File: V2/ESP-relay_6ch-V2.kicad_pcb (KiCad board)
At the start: 2 copper layers, 173 x 67.8 mm, 104 parts, among them J1 24VDC, J2 24V INPUTS, J3 OUT1, J4 OUT1, J5 OUT1, J6 OUT1, J7 OUT1, J8 OUT1, K1 G5PZ-1A, K2 G5PZ-1A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

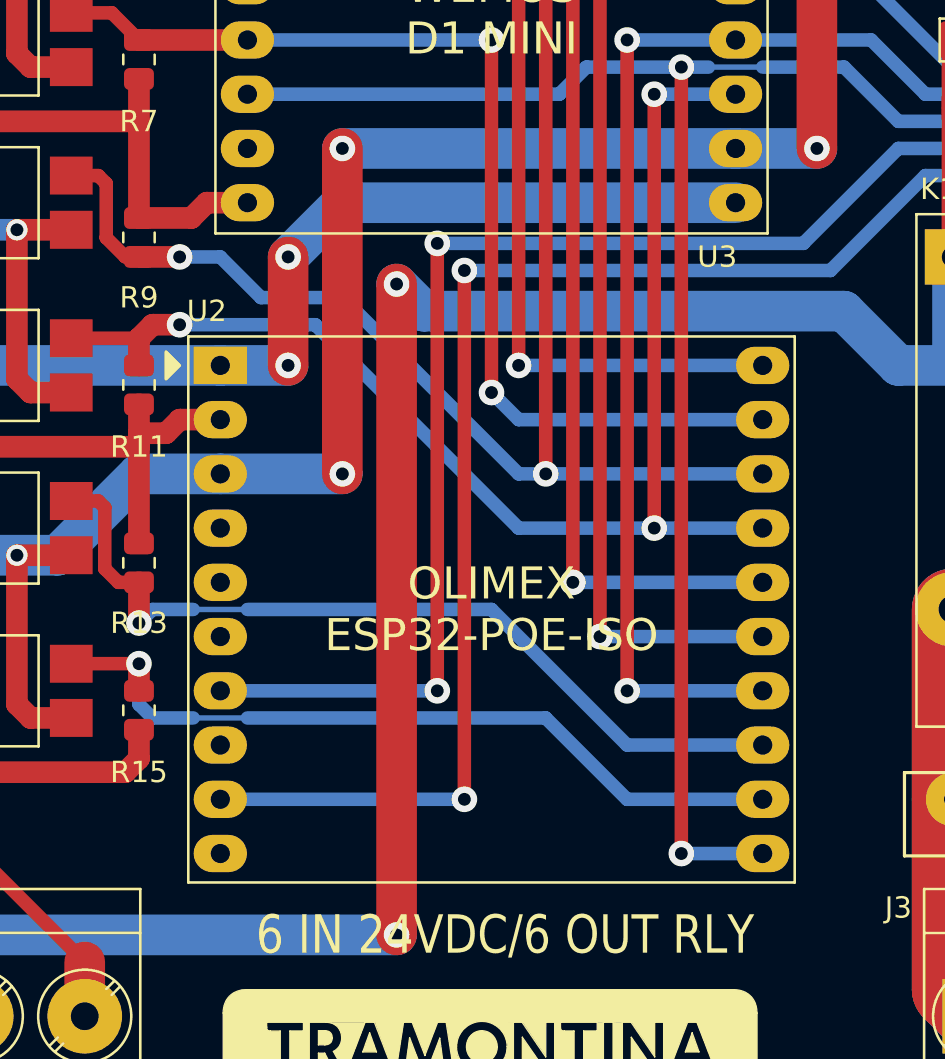
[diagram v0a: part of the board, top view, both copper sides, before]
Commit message: footprint updates
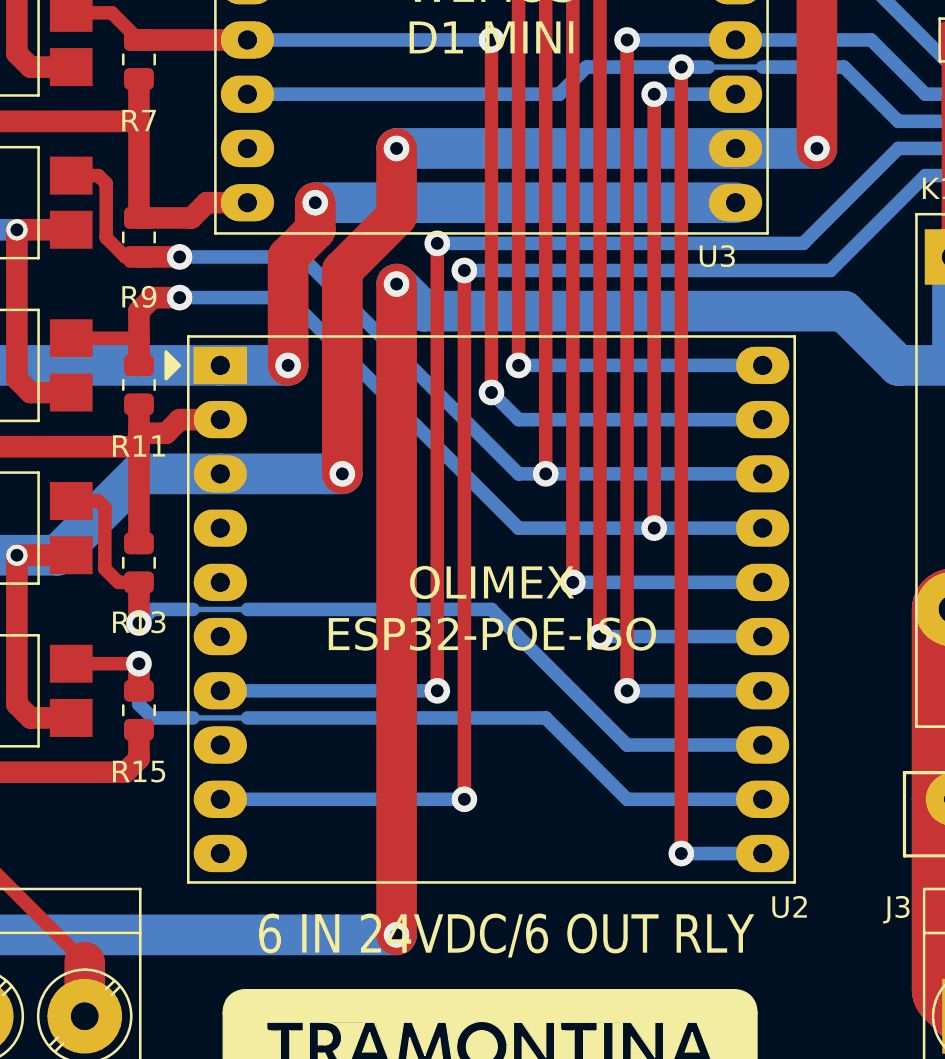
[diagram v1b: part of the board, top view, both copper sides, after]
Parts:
- U4, U5, U6, U7, U8, U9: footprint Tales:SMDIP-4_W9.53mm -> Package_DIP:SMDIP-4_W9.53mm
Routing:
- net /32-GPI34: track 62.0 -> 63.8 mm
- net GNDREF: track 440.8 -> 439.4 mm
- net +5V: track 121.0 -> 121.7 mm

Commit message: work in progress
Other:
- board text added: "6x IN 24VDC/6x OUT RLY"
- board text added: "MAX LOAD 10 A PER CHANNEL"
- board text removed: "6 IN 24VDC/6 OUT RLY"
- board text removed: "MAXIMUM 10 A PER CHANNEL"
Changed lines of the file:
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@@
     (tags "Diode Mini-MELF (SOD-80)")
     (property "Case" "MiniMELF")
-    (property "JLCPCB BOM" "0")
-    (property "Mfr" "Rectron")
+    (property "JLCPCB BOM" "1")
+    (property "LCSC Part" "C109072")
+    (property "Mfr" "Semtech")
     (property "Mfr PN" "ZMM5239B")
     (property "Sheetfile" "ESP-relay_6ch-V2.kicad_sch")
     (property "Sheetname" "")
     (property "Technology" "~")
-    (property "Vendor" "Mouser")
-    (property "Vendor PN" "583-ZMM5239B")
+    (property "Vendor" "JLCPCB")
+    (property "Vendor PN" "C109072")
     (attr smd)
     (fp_text reference "D10" (at 3.655 0 180) (layer "F.SilkS")
@@
     (tags "Diode Mini-MELF (SOD-80)")
     (property "Case" "MiniMELF")
-    (property "JLCPCB BOM" "0")
-    (property "Mfr" "Rectron")
+    (property "JLCPCB BOM" "1")
+    (property "LCSC Part" "C109072")
+    (property "Mfr" "Semtech")
     (property "Mfr PN" "ZMM5239B")
     (property "Sheetfile" "ESP-relay_6ch-V2.kicad_sch")
     (property "Sheetname" "")
     (property "Technology" "~")
-    (property "Vendor" "Mouser")
-    (property "Vendor PN" "583-ZMM5239B")
+    (property "Vendor" "JLCPCB")
+    (property "Vendor PN" "C109072")
     (attr smd)
     (fp_text reference "D7" (at 3.655 0 180) (layer "F.SilkS")
@@
     (tags "Diode Mini-MELF (SOD-80)")
     (property "Case" "MiniMELF")
-    (property "JLCPCB BOM" "0")
-    (property "Mfr" "Rectron")
+    (property "JLCPCB BOM" "1")
+    (property "LCSC Part" "C109072")
+    (property "Mfr" "Semtech")
     (property "Mfr PN" "ZMM5239B")
     (property "Sheetfile" "ESP-relay_6ch-V2.kicad_sch")
     (property "Sheetname" "")
     (property "Technology" "~")
-    (property "Vendor" "Mouser")
-    (property "Vendor PN" "583-ZMM5239B")
+    (property "Vendor" "JLCPCB")
+    (property "Vendor PN" "C109072")
     (attr smd)
     (fp_text reference "D9" (at 3.655 0 180) (layer "F.SilkS")
@@
     (tags "Diode Mini-MELF (SOD-80)")
     (property "Case" "MiniMELF")
-    (property "JLCPCB BOM" "0")
-    (property "Mfr" "Rectron")
+    (property "JLCPCB BOM" "1")
+    (property "LCSC Part" "C109072")
+    (property "Mfr" "Semtech")
     (property "Mfr PN" "ZMM5239B")
     (property "Sheetfile" "ESP-relay_6ch-V2.kicad_sch")
     (property "Sheetname" "")
     (property "Technology" "~")
-    (property "Vendor" "Mouser")
-    (property "Vendor PN" "583-ZMM5239B")
+    (property "Vendor" "JLCPCB")
+    (property "Vendor PN" "C109072")
     (attr smd)
     (fp_text reference "D8" (at 3.655 0 180) (layer "F.SilkS")
@@
     (tags "Diode Mini-MELF (SOD-80)")
     (property "Case" "MiniMELF")
-    (property "JLCPCB BOM" "0")
-    (property "Mfr" "Rectron")
+    (property "JLCPCB BOM" "1")
+    (property "LCSC Part" "C109072")
+    (property "Mfr" "Semtech")
     (property "Mfr PN" "ZMM5239B")
     (property "Sheetfile" "ESP-relay_6ch-V2.kicad_sch")
     (property "Sheetname" "")
     (property "Technology" "~")
-    (property "Vendor" "Mouser")
-    (property "Vendor PN" "583-ZMM5239B")
+    (property "Vendor" "JLCPCB")
+    (property "Vendor PN" "C109072")
     (attr smd)
     (fp_text reference "D5" (at 3.655 0 180) (layer "F.SilkS")
@@
     (tags "Diode Mini-MELF (SOD-80)")
     (property "Case" "MiniMELF")
-    (property "JLCPCB BOM" "0")
-    (property "Mfr" "Rectron")
+    (property "JLCPCB BOM" "1")
+    (property "LCSC Part" "C109072")
+    (property "Mfr" "Semtech")
     (property "Mfr PN" "ZMM5239B")
     (property "Sheetfile" "ESP-relay_6ch-V2.kicad_sch")
     (property "Sheetname" "")
     (property "Technology" "~")
-    (property "Vendor" "Mouser")
-    (property "Vendor PN" "583-ZMM5239B")
+    (property "Vendor" "JLCPCB")
+    (property "Vendor PN" "C109072")
     (attr smd)
     (fp_text reference "D6" (at 3.655 0 180) (layer "F.SilkS")
@@
   (gr_line (start 73.66 76.2) (end 88.9 76.2) (layer "F.SilkS") (width 0.15))
   (gr_rect (start 64.77 64.28) (end 237.77 132.08) (layer "Edge.Cuts") (width 0.1) (fill none))
-  (gr_text "MAXIMUM 10 A PER CHANNEL" (at 193.675 97.79) (layer "B.Cu")
-    (effects (font (size 2.8 2.5) (thickness 0.4)) (justify mirror))
-  )
   (gr_text "-" (at 78.74 130.302) (layer "F.SilkS")
     (effects (font (size 2 2) (thickness 0.5)))
@@
     (effects (font (size 1.8 1.6) (thickness 0.3)) (justify left))
   )
-  (gr_text "6 IN 24VDC/6 OUT RLY" (at 133.985 119.38) (layer "F.SilkS")
+  (gr_text "MAX LOAD 10 A PER CHANNEL" (at 193.04 67.945) (layer "F.SilkS")
+    (effects (font (size 2.3 2) (thickness 0.3)))
+  )
+  (gr_text "6x IN 24VDC/6x OUT RLY" (at 133.985 119.38) (layer "F.SilkS")
     (effects (font (size 1.8 1.5) (thickness 0.3)))
   )

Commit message: wip
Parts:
- removed the J1 at (72.4, 123.2)
- removed REF**: Logo_Tramontina_25mm, Tales:Logo_Tramontina_25mm
- J1: renamed from J2; value 24V INPUTS -> POWER & INPUTS; footprint Tales:TerminalBlock_Phoenix_MKDS-3-6-5.08_1x06_P5.08mm_Horizontal -> Tales:TerminalBlock_Phoenix_MKDS-3-8-5.08_1x08_P5.08mm_Horizontal
- moved C2 19.3 mm to (74.5, 82.5)
- moved J1 11.4 mm to (78.7, 118.1)
- moved D1 5.24 mm to (83.8, 108.8)
- moved R28 5.24 mm to (80.4, 109.2)
- moved R29 5.24 mm to (80.4, 106.7)
- moved R30 5.24 mm to (76.6, 109.2)
- moved R31 5.24 mm to (76.6, 106.7)
- moved R32 5.24 mm to (72.7, 109.2)
- moved R33 5.24 mm to (72.7, 106.7)
- moved R34 5.24 mm to (68.9, 109.2)
- moved R35 5.24 mm to (68.9, 106.7)
- moved D23 5.08 mm to (72.0, 101.6)
- moved D24 5.08 mm to (79.6, 101.6)
- moved J2 5.08 mm to (156.2, 118.1)
- moved J3 5.08 mm to (170.2, 118.1)
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- renumbered J3 to J2, J4 to J3, J5 to J4, J6 to J5, J7 to J6, J8 to J7
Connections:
- J1 pad 1: Net-(J2-Pad1) (its old number) -> +24V
- J1 pad 2: Net-(J2-Pad2) (its old number) -> GNDREF
- J1 pad 3: Net-(J2-Pad3) -> Net-(J1-Pad3)
- J1 pad 4: Net-(J2-Pad4) -> Net-(J1-Pad4)
- J1 pad 5: Net-(J2-Pad5) -> Net-(J1-Pad5)
- J1 pad 6: Net-(J2-Pad6) -> Net-(J1-Pad6)
- R10 pad 2: Net-(J2-Pad4) -> Net-(J1-Pad6)
- R12 pad 2: Net-(J2-Pad5) -> Net-(J1-Pad7)
- R14 pad 2: Net-(J2-Pad6) -> Net-(J1-Pad8)
- R4 pad 2: Net-(J2-Pad1) (its old number) -> Net-(J1-Pad3)
- R6 pad 2: Net-(J2-Pad2) (its old number) -> Net-(J1-Pad4)
- R8 pad 2: Net-(J2-Pad3) -> Net-(J1-Pad5)
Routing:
- net Net-(J2-Pad1) (its old number): track 61.3 -> 0.00 mm
- net Net-(J1-Pad3): track 0.00 -> 56.2 mm
- net Net-(J2-Pad2) (its old number): track 50.1 -> 0.00 mm
- net Net-(J2-Pad3): track 48.1 -> 0.00 mm
- net Net-(J1-Pad4): track 0.00 -> 45.1 mm
- net Net-(J1-Pad5): track 0.00 -> 43.8 mm
- net Net-(J2-Pad4): track 38.5 -> 0.00 mm
- net Net-(J2-Pad5): track 37.2 -> 0.00 mm
- net Net-(J1-Pad6): track 0.00 -> 34.9 mm
- net Net-(J1-Pad7): track 0.00 -> 34.8 mm
- net Net-(J2-Pad6): track 26.5 -> 0.00 mm
- net Net-(J1-Pad8): track 0.00 -> 24.8 mm
- net GNDREF: track 439.4 -> 425.9 mm
- net Net-(J7-Pad2): track 32.1 -> 27.0 mm
- net Net-(J6-Pad2): track 32.1 -> 27.0 mm
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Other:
- board text added: "MAX LOAD 10A/CHANNEL"
- board text removed: "MAX LOAD 10 A PER CHANNEL"

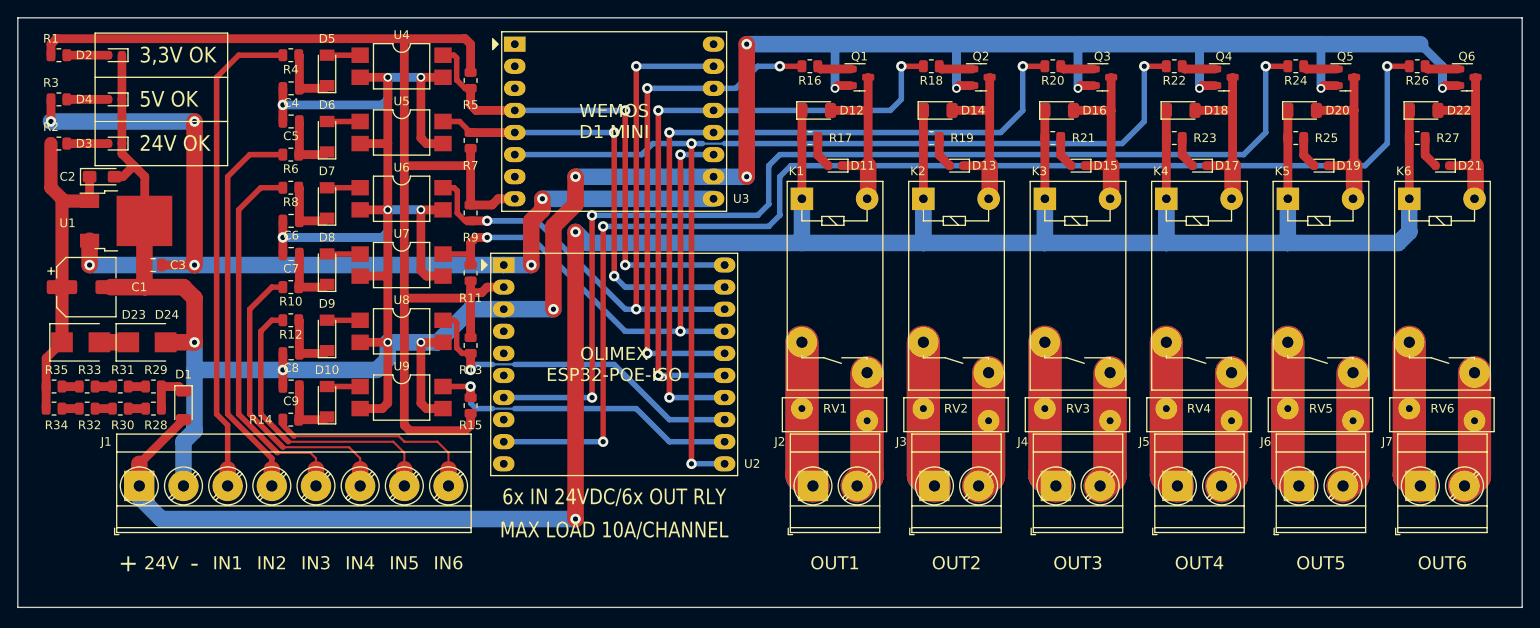
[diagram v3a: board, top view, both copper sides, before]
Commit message: add pull down resistors
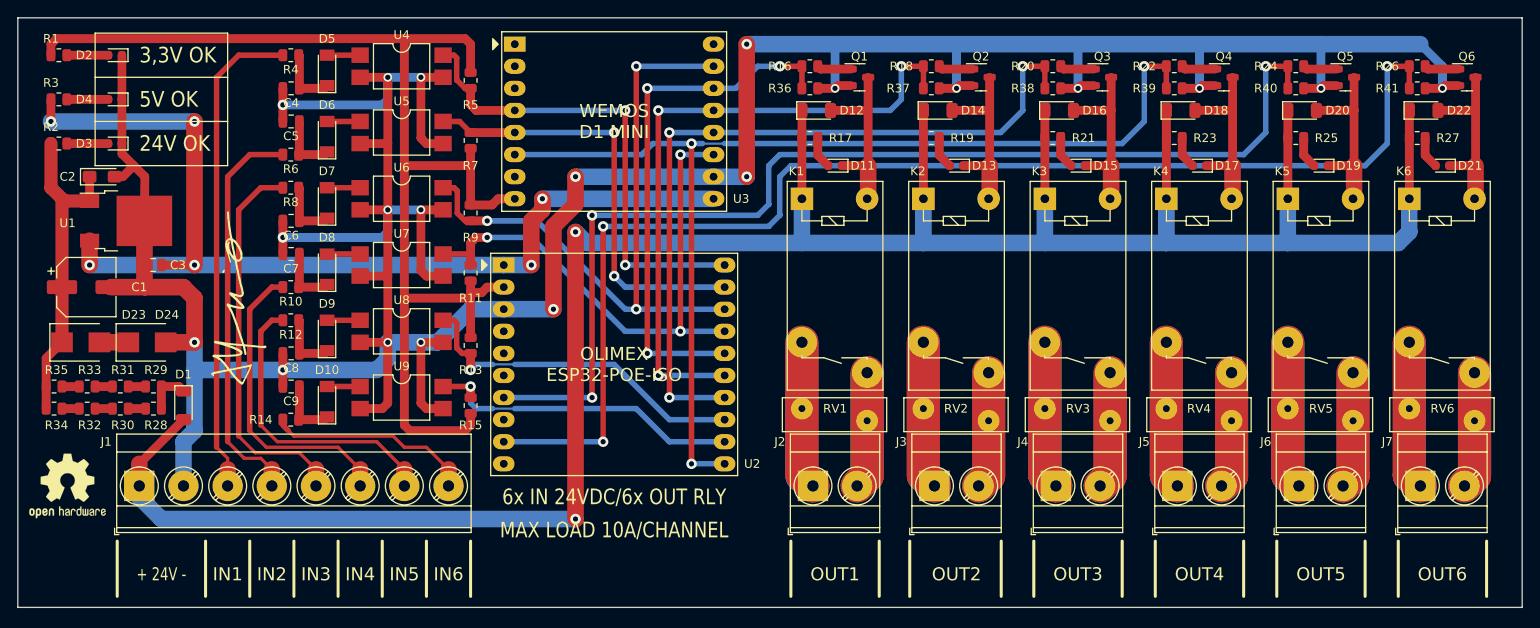
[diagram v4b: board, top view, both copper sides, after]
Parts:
- added ?: , Tales:TMaschio_20x6.4mm, F.Cu at (90.2, 96.5)
- added R36: 10k/0,125W/0805, Tales:R_0805_2012Metric, F.Cu at (155.9, 72.4)
- added R37: 10k/0,125W/0805, Tales:R_0805_2012Metric, F.Cu at (169.8, 72.4)
- added R38: 10k/0,125W/0805, Tales:R_0805_2012Metric, F.Cu at (183.8, 72.4)
- added R39: 10k/0,125W/0805, Tales:R_0805_2012Metric, F.Cu at (197.8, 72.4)
- added R40: 10k/0,125W/0805, Tales:R_0805_2012Metric, F.Cu at (211.7, 72.4)
- added R41: 10k/0,125W/0805, Tales:R_0805_2012Metric, F.Cu at (225.7, 72.4)
- added REF**: OSHW-Logo2_9.8x8mm_SilkScreen, Symbol:OSHW-Logo2_9.8x8mm_SilkScreen, F.Cu at (70.5, 118.1)
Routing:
- net GNDREF: track 425.9 -> 437.8 mm
- net /32-GPIO4: track 144.3 -> 146.9 mm
- net /32-GPIO32: track 72.9 -> 75.5 mm
- net /32-GPIO33: track 58.2 -> 60.7 mm
- net /32-GPIO2: track 125.3 -> 127.8 mm
- net /32-GPIO16: track 86.1 -> 88.7 mm
- net /32-GPIO13: track 123.5 -> 126.0 mm
- net Net-(J1-Pad8): track 24.8 -> 23.7 mm
- net Net-(J1-Pad4): track 45.1 -> 46.2 mm
- net Net-(J1-Pad5): track 43.8 -> 44.5 mm
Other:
- board text added: "+ 24V -"
- board text removed: "+"
- board text removed: "-"
- board text removed: "24V"

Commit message: Updates
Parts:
- added R42: 4k7/0,125W/0805, Tales:R_0805_2012Metric, F.Cu at (117.8, 67.3)
- moved ? 49.5 mm to (133.3, 120.7), turned to 0 degrees
- moved REF** 36.7 mm to (88.9, 86.4)
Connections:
- net /32-GPI34 renamed IN4
- net /32-GPI35 renamed IN3
- net /32-GPI36 renamed IN2
- net /32-GPI39 renamed IN1
- net /32-GPIO13 renamed OUT4
- net /32-GPIO14 renamed IN6
- net /32-GPIO15 renamed IN5
- net /32-GPIO16 renamed OUT3
- net /32-GPIO2 renamed OUT5
- net /32-GPIO32 renamed OUT2
- net /32-GPIO33 renamed OUT1
- net /32-GPIO4 renamed OUT6
- U2 pad 4: unconnected-(U2-Pad4) -> Net-(U2-Pad4)
- U3 pad 1: unconnected-(U3-Pad1) -> Net-(U2-Pad4)
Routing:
- net Net-(U2-Pad4): track 0.00 -> 55.3 mm, vias 0 -> 2
- net OUT6: track 146.9 -> 148.7 mm

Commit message: PCB tweaks
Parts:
- U4, U5, U6, U7, U8, U9: footprint Package_DIP:SMDIP-4_W9.53mm -> Tales:SMDIP-4_W9.53mm
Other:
- board text added: "V~ LOAD"
